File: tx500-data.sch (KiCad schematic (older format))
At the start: 62 parts, among them J1 USB_C_Receptacle, J2 FTDI, J3 AUDIO, SW1 VCCIO, U1 TUSB2036, U2 FT232RL, U3 HS-100B, U4 TPS76333, U5 SN75240, U6 TPS2041, Y1 AWSCR-6.00CPLA

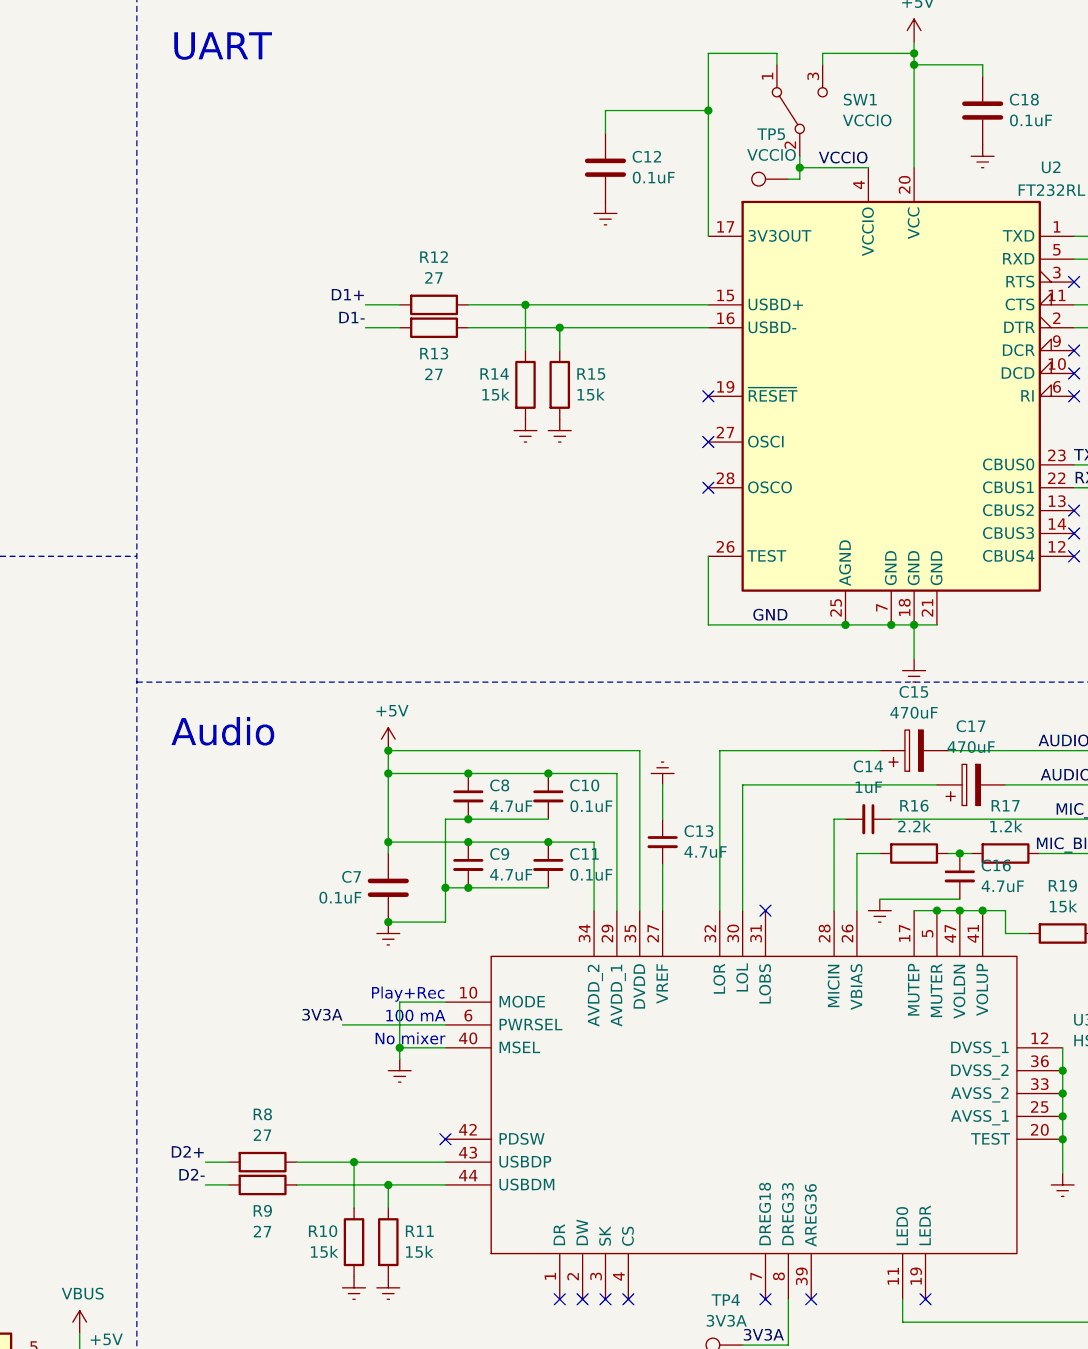
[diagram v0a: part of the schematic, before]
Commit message: Route most of the board
Still need to check design rules
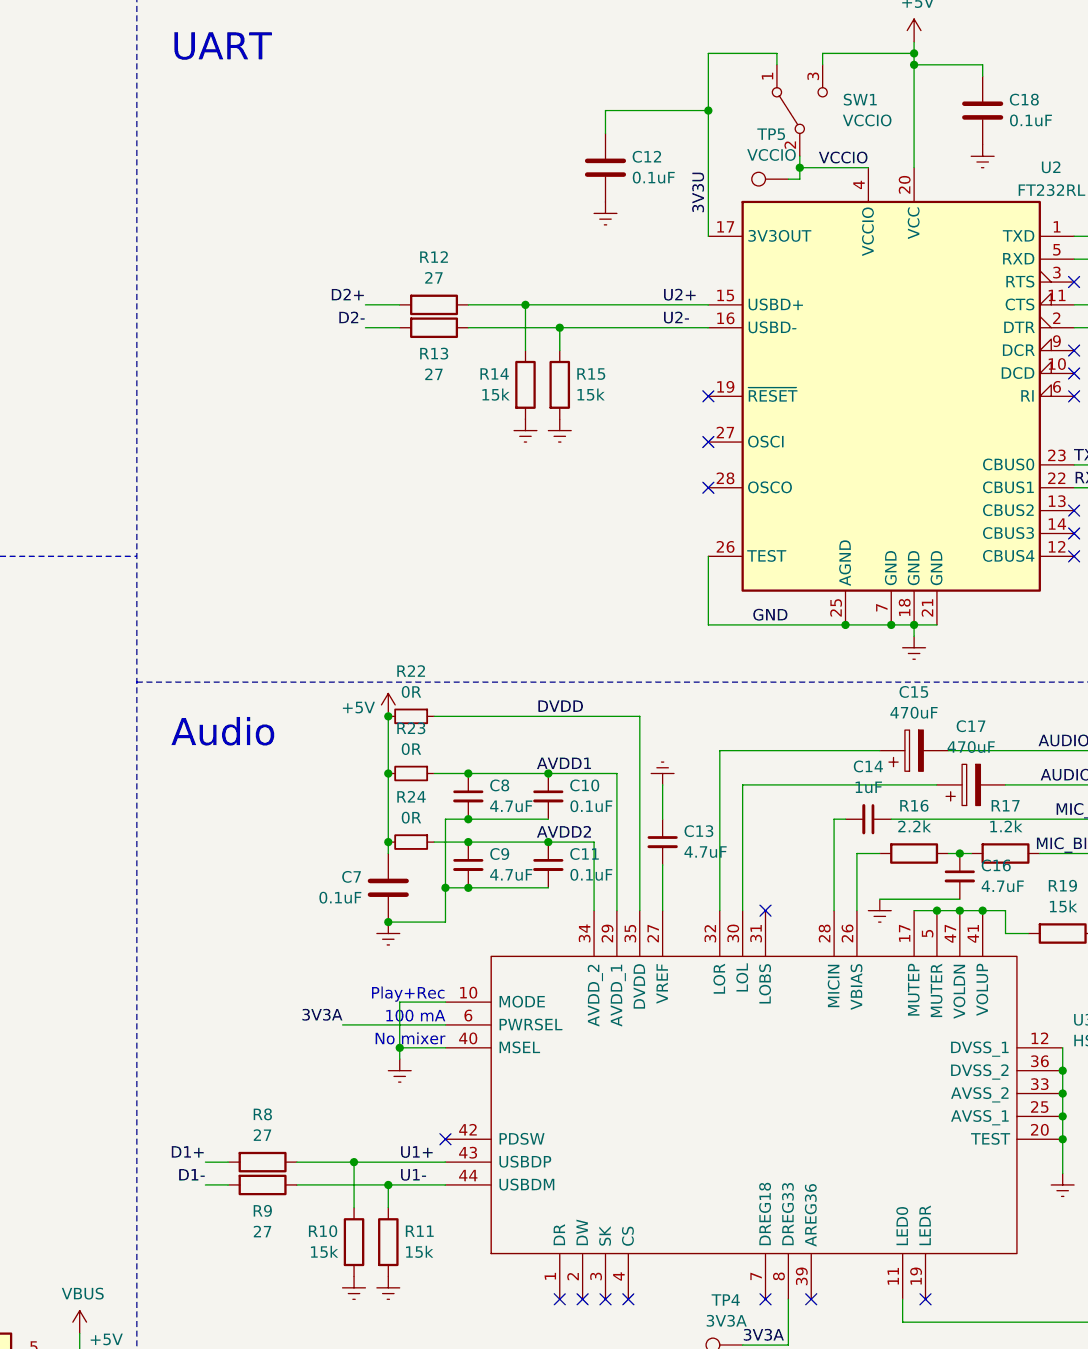
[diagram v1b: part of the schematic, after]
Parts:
- added R22, R23, R24: 0R, Resistor_SMD:R_0603_1608Metric, symbol Device:R_Small
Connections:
- net +5V: now also R22.2, R23.2, R24.2; no longer C10.1, C11.1, C8.1, C9.1, U3.29 (AVDD_1), U3.34 (AVDD_2), U3.35 (DVDD)
- net D1+: now also R8.2; no longer R12.2
- net D1-: now also R9.2; no longer R13.2
- net D2+: now also R12.2; no longer R8.2
- net D2-: now also R13.2; no longer R9.2
- net U2+: now reaches R12.1, R14.1, U2.15 (USBD+)
- net U2-: now reaches R13.1, R15.1, U2.16 (USBD-)
- net U1+: now reaches R10.1, R8.1, U3.43 (USBDP)
- net U1-: now reaches R11.1, R9.1, U3.44 (USBDM)
- net 3V3U: now reaches C12.1, SW1.1 (A), U2.17 (3V3OUT)
- new net AVDD1: C10.1, C8.1, R23.1, U3.29 (AVDD_1)
- new net AVDD2: C11.1, C9.1, R24.1, U3.34 (AVDD_2)
- new net DVDD: R22.1, U3.35 (DVDD)
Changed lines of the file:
@@
 L power:GNDREF #PWR?
 U 1 1 605FD4DB
-P 8950 3400
+P 8950 3300
 AR Path="/6059C0E9/605FD4DB" Ref="#PWR?"  Part="1"
 AR Path="/605FD4DB" Ref="#PWR033"  Part="1"
-F 0 "#PWR033" H 8950 3150 50  0001 C CNN
-F 1 "GNDREF" H 8955 3227 50  0001 C CNN
-F 2 "" H 8950 3400 50  0001 C CNN
-F 3 "" H 8950 3400 50  0001 C CNN
-	1    8950 3400
+F 0 "#PWR033" H 8950 3050 50  0001 C CNN
+F 1 "GNDREF" H 8955 3127 50  0001 C CNN
+F 2 "" H 8950 3300 50  0001 C CNN
+F 3 "" H 8950 3300 50  0001 C CNN
+	1    8950 3300
 	1    0    0    -1
 $EndComp
@@
 Text Label 10650 1550 2    50   ~ 0
 GND
-Text Label 6550 1950 2    50   ~ 0
+Text Label 5850 5700 2    50   ~ 0
 D1-
-Text Label 6550 1850 2    50   ~ 0
+Text Label 5850 5600 2    50   ~ 0
 D1+
 Text Label 4000 5600 0    50   ~ 0
@@
 Text Label 10550 4350 2    50   ~ 0
 MIC_IN
-Text Label 5850 5600 2    50   ~ 0
+Text Label 6550 1850 2    50   ~ 0
 D2+
-Text Label 5850 5700 2    50   ~ 0
+Text Label 6550 1950 2    50   ~ 0
 D2-
 Text Notes 5700 3800 0    118  ~ 0
@@
 	6250 5600 6500 5600
 Wire Wire Line
-	8950 3250 8950 3400
-Wire Wire Line
-	6650 3800 6650 3900
+	8950 3250 8950 3300
+Wire Wire Line
+	6650 3650 6650 3900
 Wire Wire Line
 	8400 6400 8200 6400
@@
 L power:+5V #PWR023
 U 1 1 609E6767
-P 6650 3800
-F 0 "#PWR023" H 6650 3650 50  0001 C CNN
-F 1 "+5V" H 6665 3973 50  0000 C CNN
-F 2 "" H 6650 3800 50  0001 C CNN
-F 3 "" H 6650 3800 50  0001 C CNN
-	1    6650 3800
+P 6650 3650
+F 0 "#PWR023" H 6650 3500 50  0001 C CNN
+F 1 "+5V" H 6592 3687 50  0000 R CNN
+F 2 "" H 6650 3650 50  0001 C CNN
+F 3 "" H 6650 3650 50  0001 C CNN
+	1    6650 3650
 	1    0    0    -1
 $EndComp
@@
 	9350 3950 9800 3950
 Wire Wire Line
-	6650 3800 7750 3800
-Wire Wire Line
-	7750 3800 7750 4500
-Connection ~ 6650 3800
+	7750 3650 7750 4500
+Connection ~ 6650 3650
 Text Label 9800 4100 2    50   ~ 0
 MIC_IN
@@
 	1    0    0    -1
 $EndComp
-Wire Wire Line
-	6650 3900 7000 3900
 Connection ~ 7000 3900
 Wire Wire Line
@@
 	1    0    0    -1
 $EndComp
-Wire Wire Line
-	6650 4200 7000 4200
 Wire Wire Line
 	7550 4200 7550 4500
@@
 $EndComp
 Connection ~ 5400 6650
+$Comp
+L Device:R_Small R22
+U 1 1 60953C75
+P 6750 3650
+F 0 "R22" V 6554 3650 50  0000 C CNN
+F 1 "0R" V 6645 3650 50  0000 C CNN
+F 2 "Resistor_SMD:R_0603_1608Metric" H 6750 3650 50  0001 C CNN
+F 3 "~" H 6750 3650 50  0001 C CNN
+	1    6750 3650
+	0    1    1    0
+$EndComp
+Wire Wire Line
+	6850 3650 7750 3650
+$Comp
+L Device:R_Small R23
+U 1 1 609546BE
+P 6750 3900
+F 0 "R23" V 6554 3900 50  0000 C CNN
+F 1 "0R" V 6645 3900 50  0000 C CNN
+F 2 "Resistor_SMD:R_0603_1608Metric" H 6750 3900 50  0001 C CNN
+F 3 "~" H 6750 3900 50  0001 C CNN
+	1    6750 3900
+	0    1    1    0
+$EndComp
+Wire Wire Line
+	6850 3900 7000 3900
+$Comp
+L Device:R_Small R24
+U 1 1 60954ABD
+P 6750 4200
+F 0 "R24" V 6554 4200 50  0000 C CNN
+F 1 "0R" V 6645 4200 50  0000 C CNN
+F 2 "Resistor_SMD:R_0603_1608Metric" H 6750 4200 50  0001 C CNN
+F 3 "~" H 6750 4200 50  0001 C CNN
+	1    6750 4200
+	0    1    1    0
+$EndComp
+Wire Wire Line
+	6850 4200 7000 4200
+Text Label 7300 3650 0    50   ~ 0
+DVDD
+Text Label 7300 3900 0    50   ~ 0
+AVDD1
+Text Label 7300 4200 0    50   ~ 0
+AVDD2
+Text Label 7850 1850 0    50   ~ 0
+U2+
+Text Label 7850 1950 0    50   ~ 0
+U2-
+Text Label 6700 5600 0    50   ~ 0
+U1+
+Text Label 6700 5700 0    50   ~ 0
+U1-
+Text Label 8050 1450 1    50   ~ 0
+3V3U
 $EndSCHEMATC

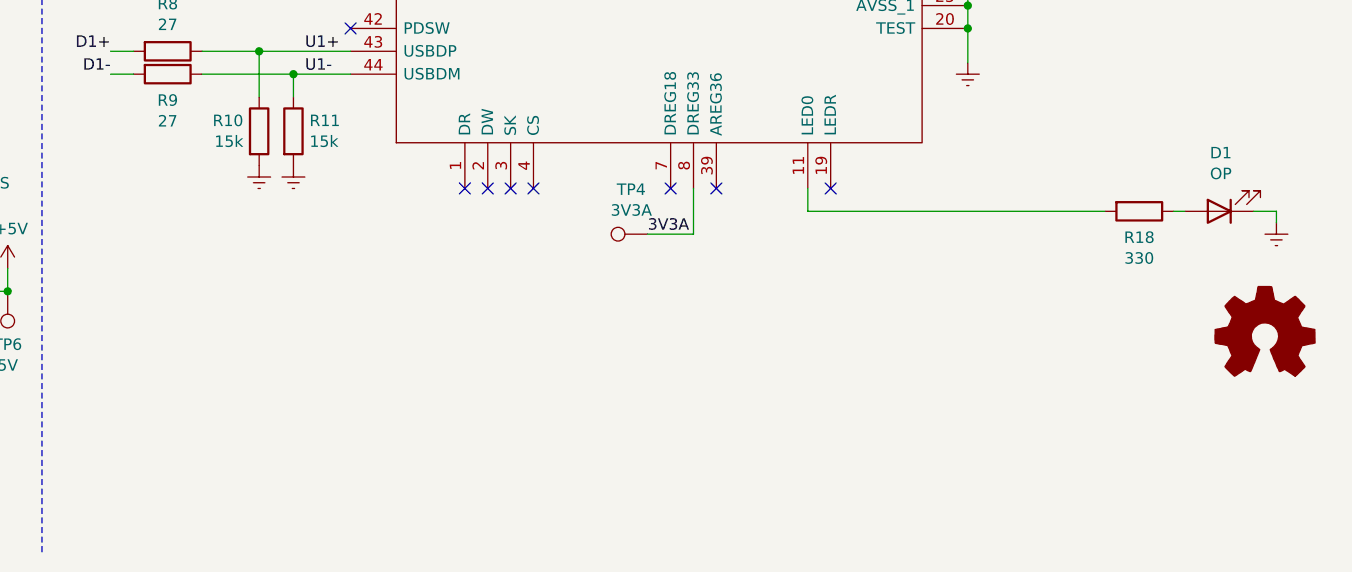
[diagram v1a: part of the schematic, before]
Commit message: Rotate UART and fix 3D images
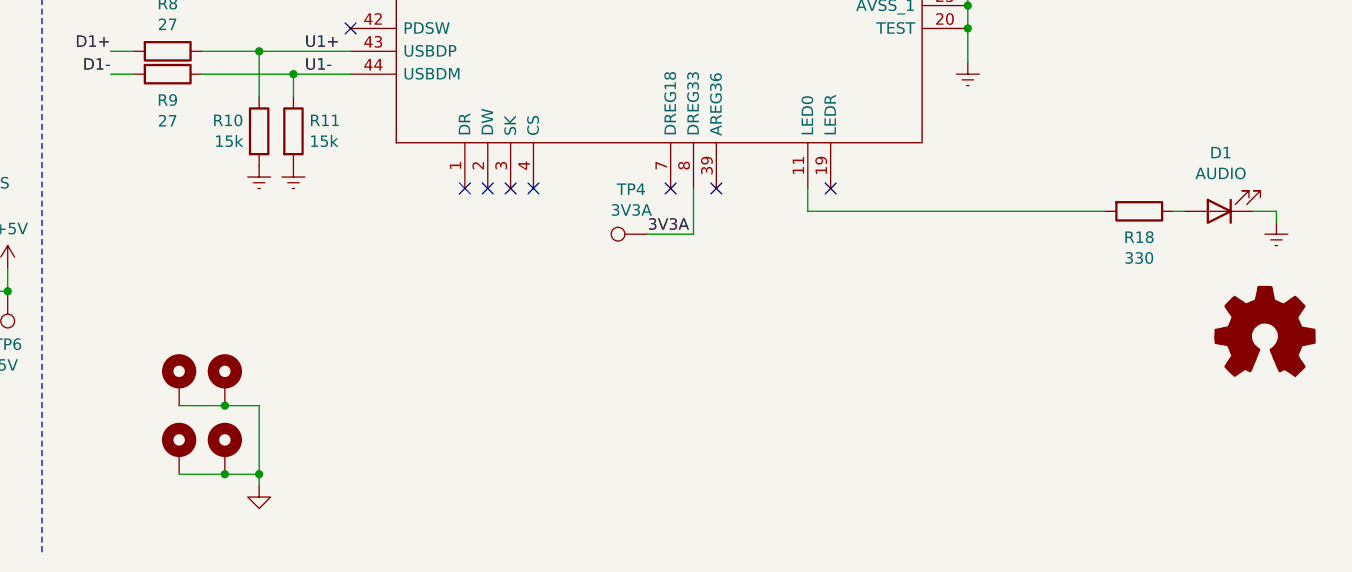
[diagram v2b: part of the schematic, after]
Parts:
- added H1, H2, H3, H4: MountingHole_Pad, MountingHole:MountingHole_2.2mm_M2_Pad, symbol Mechanical:MountingHole_Pad
- D1: value OP -> AUDIO
- J1: footprint CUI:UJ31-CH-G-SMT-TR-67 -> CUI:CUI_UJ31-CH-G-SMT-TR-67
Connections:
- net GND1: now also H1.1, H2.1, H3.1, H4.1
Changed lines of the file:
@@
 F 0 "J1" H 2307 2367 50  0000 C CNN
 F 1 "USB_C_Receptacle" H 2307 2276 50  0000 C CNN
-F 2 "CUI:UJ31-CH-G-SMT-TR-67" H 2350 1500 50  0001 C CNN
+F 2 "CUI:CUI_UJ31-CH-G-SMT-TR-67" H 2350 1500 50  0001 C CNN
 F 3 "https://www.mouser.com/datasheet/2/670/uj31_ch_g_smt_tr_67-2306975.pdf" H 2350 1500 50  0001 C CNN
 F 4 "CUI" H 2200 1500 50  0001 C CNN "Manufacturer"
@@
 P 10700 6300
 F 0 "D1" H 10693 6045 50  0000 C CNN
-F 1 "OP" H 10693 6136 50  0000 C CNN
+F 1 "AUDIO" H 10693 6136 50  0000 C CNN
 F 2 "LED_SMD:LED_0603_1608Metric" H 10700 6300 50  0001 C CNN
 F 3 "" H 10700 6300 50  0001 C CNN
@@
 Text Label 8050 1450 1    50   ~ 0
 3V3U
+$Comp
+L Mechanical:MountingHole_Pad H3
+U 1 1 6098967B
+P 6350 7050
+F 0 "H3" H 6350 7337 50  0001 C CNN
+F 1 "MountingHole_Pad" H 6350 7246 50  0001 C CNN
+F 2 "MountingHole:MountingHole_2.2mm_M2_Pad" H 6350 7050 50  0001 C CNN
+F 3 "~" H 6350 7050 50  0001 C CNN
+	1    6350 7050
+	1    0    0    -1
+$EndComp
+$Comp
+L Mechanical:MountingHole_Pad H1
+U 1 1 60989F62
+P 6150 7050
+F 0 "H1" H 6250 7099 50  0001 L CNN
+F 1 "MountingHole_Pad" H 6250 7008 50  0001 L CNN
+F 2 "MountingHole:MountingHole_2.2mm_M2_Pad" H 6150 7050 50  0001 C CNN
+F 3 "~" H 6150 7050 50  0001 C CNN
+	1    6150 7050
+	1    0    0    -1
+$EndComp
+$Comp
+L Mechanical:MountingHole_Pad H4
+U 1 1 6098A40D
+P 6350 7350
+F 0 "H4" H 6450 7399 50  0001 L CNN
+F 1 "MountingHole_Pad" H 6450 7308 50  0001 L CNN
+F 2 "MountingHole:MountingHole_2.2mm_M2_Pad" H 6350 7350 50  0001 C CNN
+F 3 "~" H 6350 7350 50  0001 C CNN
+	1    6350 7350
+	1    0    0    -1
+$EndComp
+$Comp
+L Mechanical:MountingHole_Pad H2
+U 1 1 6098A95D
+P 6150 7350
+F 0 "H2" H 6250 7399 50  0001 L CNN
+F 1 "MountingHole_Pad" H 6250 7308 50  0001 L CNN
+F 2 "MountingHole:MountingHole_2.2mm_M2_Pad" H 6150 7350 50  0001 C CNN
+F 3 "~" H 6150 7350 50  0001 C CNN
+	1    6150 7350
+	1    0    0    -1
+$EndComp
+$Comp
+L power:GND1 #PWR0101
+U 1 1 60990A0B
+P 6500 7500
+F 0 "#PWR0101" H 6500 7250 50  0001 C CNN
+F 1 "GND1" H 6505 7327 50  0001 C CNN
+F 2 "" H 6500 7500 50  0001 C CNN
+F 3 "" H 6500 7500 50  0001 C CNN
+	1    6500 7500
+	1    0    0    -1
+$EndComp
+Wire Wire Line
+	6150 7150 6350 7150
+Wire Wire Line
+	6500 7150 6500 7450
+Connection ~ 6350 7150
+Wire Wire Line
+	6350 7150 6500 7150
+Wire Wire Line
+	6150 7450 6350 7450
+Connection ~ 6500 7450
+Wire Wire Line
+	6500 7450 6500 7500
+Connection ~ 6350 7450
+Wire Wire Line
+	6350 7450 6500 7450
 $EndSCHEMATC

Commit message: Start prepping fabrication
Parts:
- C1, C12, C3: Description - -> (none); LCSC (none) -> C1588
- C10, C11, C18, C7: LCSC (none) -> C1588
- C13, C16, C8, C9: LCSC (none) -> C19666
- C14: LCSC (none) -> C15849
- C15, C17, H1, H2, H3, H4, J2, J3, LOGO1, SW1, TP1, TP2, TP3, TP4, TP5, TP6, U1, U4, U5: LCSC (none) -> -
- C2, C4: Description - -> (none); LCSC (none) -> C19666
- C5, C6: Description - -> (none); LCSC (none) -> C1653
- D1, D2, D3: LCSC (none) -> C2286
- J1: LCSC (none) -> -; Manufacturer CUI -> (none); Manufacturer_Name (none) -> CUI; Manufacturer_Part_Number (none) -> UJ31-CH-G-SMT-TR-67; Mfg Part # UJ31-CH-G-SMT-TR-67 -> (none)
- L1, L2: footprint Inductor_SMD:L_0603_1608Metric -> Inductor_SMD:L_0805_2012Metric; LCSC (none) -> C1017
- R1, R10, R11, R14, R15, R19: Description - -> (none); LCSC (none) -> C22809
- R12, R13, R6, R7, R8, R9: Description - -> (none); LCSC (none) -> C25190
- R16: Description - -> (none); LCSC (none) -> C4190
- R17: Description - -> (none); LCSC (none) -> C22765
- R18, R20, R21: LCSC (none) -> C23137
- R2, R3: Description - -> (none); LCSC (none) -> C22843
- R22, R23, R24: LCSC (none) -> C21189
- R4, R5: LCSC (none) -> C23186
- U2: LCSC (none) -> C8690
- U3: Height 1.6 -> (none); LCSC (none) -> -
- U6: Description (none) -> Overcurrent protection; LCSC (none) -> -
- Y1: Description Resonators 6.0 MHZ 30PF -> Resonator 6 MHz; Height 1.7 -> (none); LCSC (none) -> -; Mouser Part Number 815-CR-6.00CPLA-30-T -> (none); Mouser Price/Stock https://www.mouser.co.uk/ProductDetail/ABRACON/AWSCR-600CPL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 -> (none)

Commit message: Add more LCSC part numbers
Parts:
- C15, C17: LCSC - -> C232200
- J2, J3: LCSC - -> C471518
- SW1: LCSC - -> C221660
- U1: LCSC - -> C43665
- U3: LCSC - -> C371351
- U4: LCSC - -> C7100
- U5: LCSC - -> C7067
- U6: LCSC - -> C206041
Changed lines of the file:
@@
 F 9 "" H 3000 7781 50  0001 C CNN "Vendor"
 F 10 "" H 3550 7600 50  0001 C CNN "quantity"
-F 11 "-" H 3000 5900 50  0001 C CNN "LCSC"
+F 11 "C43665" H 3000 5900 50  0001 C CNN "LCSC"
 	1    3000 5900
 	1    0    0    -1
@@
 F 9 "" H 3350 4142 50  0001 C CNN "Vendor"
 F 10 "" H 3350 4142 50  0001 C CNN "quantity"
-F 11 "-" H 3350 3700 50  0001 C CNN "LCSC"
+F 11 "C7100" H 3350 3700 50  0001 C CNN "LCSC"
 	1    3350 3700
 	1    0    0    -1
@@
 F 10 "" H 7500 6750 50  0001 C CNN "Vendor"
 F 11 "" H 8921 4356 50  0001 C CNN "quantity"
-F 12 "-" H 7700 6200 50  0001 C CNN "LCSC"
+F 12 "C371351" H 7700 6200 50  0001 C CNN "LCSC"
 	1    7700 6200
 	0    -1   -1   0
@@
 F 9 "" H 3700 2725 50  0001 C CNN "Vendor"
 F 10 "" H 3700 2725 50  0001 C CNN "quantity"
-F 11 "-" H 3700 2400 50  0001 C CNN "LCSC"
+F 11 "C7067" H 3700 2400 50  0001 C CNN "LCSC"
 	1    3700 2400
 	1    0    0    -1
@@
 F 5 "TPS2041CDBV" H 4700 6650 50  0001 C CNN "Manufacturer_Part_Number"
 F 6 "Overcurrent protection" H 4700 6650 50  0001 C CNN "Description"
-F 7 "-" H 4700 6650 50  0001 C CNN "LCSC"
+F 7 "C206041" H 4700 6650 50  0001 C CNN "LCSC"
 	1    4700 6650
 	1    0    0    -1
@@
 F 2 "Connector_JST:JST_PH_B6B-PH-SM4-TB_1x06-1MP_P2.00mm_Vertical" H 10850 1750 50  0001 C CNN
 F 3 "" H 10850 1750 50  0001 C CNN
-F 4 "-" H 10850 1750 50  0001 C CNN "LCSC"
+F 4 "C471518" H 10850 1750 50  0001 C CNN "LCSC"
 	1    10850 1750
 	1    0    0    -1
@@
 F 2 "Connector_JST:JST_PH_B6B-PH-SM4-TB_1x06-1MP_P2.00mm_Vertical" H 10750 4050 50  0001 C CNN
 F 3 "" H 10750 4050 50  0001 C CNN
-F 4 "-" H 10750 4050 50  0001 C CNN "LCSC"
+F 4 "C471518" H 10750 4050 50  0001 C CNN "LCSC"
 	1    10750 4050
 	1    0    0    -1
@@
 F 2 "Button_Switch_SMD:SW_SPDT_CK-JS102011SAQN" H 8450 1000 50  0001 C CNN
 F 3 "" H 8450 1000 50  0001 C CNN
-F 4 "-" H 8450 1000 50  0001 C CNN "LCSC"
+F 4 "C221660" H 8450 1000 50  0001 C CNN "LCSC"
 	1    8450 1000
 	0    -1   -1   0
@@
 F 2 "Vishay:CAPPM7343X430N" H 8988 3650 50  0001 C CNN
 F 3 "" H 8950 3800 50  0001 C CNN
-F 4 "-" H 8950 3800 50  0001 C CNN "LCSC"
+F 4 "C232200" H 8950 3800 50  0001 C CNN "LCSC"
 	1    8950 3800
 	0    -1   -1   0
@@
 F 2 "Vishay:CAPPM7343X430N" H 9238 3800 50  0001 C CNN
 F 3 "" H 9200 3950 50  0001 C CNN
-F 4 "-" H 9200 3950 50  0001 C CNN "LCSC"
+F 4 "C232200" H 9200 3950 50  0001 C CNN "LCSC"
 	1    9200 3950
 	0    -1   -1   0

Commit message: Add BOM
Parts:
- C1, C10, C11, C12, C18, C3, C7: Vendor (none) -> LCSC; Vendor Part Number (none) -> C1588
- C13, C16, C2, C4, C8, C9: Vendor (none) -> LCSC; Vendor Part Number (none) -> C19666
- C14: Vendor (none) -> LCSC; Vendor Part Number (none) -> C15849
- C15, C17: Manufacturer_Name (none) -> Vishay; Manufacturer_Part_Number (none) -> 293D477X9010E2TE3; Vendor (none) -> Mouser; Vendor Part Number (none) -> 74-293D477X9010E2TE3
- C5, C6: Vendor (none) -> LCSC; Vendor Part Number (none) -> C1653
- D1, D2, D3: Vendor (none) -> LCSC; Vendor Part Number (none) -> C2286
- H1, H2, H3, H4, LOGO1, TP1, TP2, TP3, TP4, TP5, TP6: Manufacturer_Name (none) -> -; Manufacturer_Part_Number (none) -> -; Vendor (none) -> -; Vendor Part Number (none) -> -
- J1: Vendor (none) -> Mouser; Vendor Part Number (none) -> 490-UJ31-CH-GSMTTR67
- J2, J3: Manufacturer_Name (none) -> JST; Manufacturer_Part_Number (none) -> B6B-PH-SM4-TB; Vendor (none) -> Newark; Vendor Part Number (none) -> 37K9975
- L1, L2: Vendor (none) -> LCSC; Vendor Part Number (none) -> C1017
- R1, R10, R11, R14, R15, R19: Vendor (none) -> LCSC; Vendor Part Number (none) -> C22809
- R12, R13, R6, R7, R8, R9: value 27 -> 27R; Vendor (none) -> LCSC; Vendor Part Number (none) -> C25190
- R16: Vendor (none) -> LCSC; Vendor Part Number (none) -> C4190
- R17: Vendor (none) -> LCSC; Vendor Part Number (none) -> C22765
- R18, R20, R21: value 330 -> 330R; Vendor (none) -> LCSC; Vendor Part Number (none) -> C23137
- R2, R3: Vendor (none) -> LCSC; Vendor Part Number (none) -> C22843
- R22, R23, R24: Vendor (none) -> LCSC; Vendor Part Number (none) -> C21189
- R4, R5: Vendor (none) -> LCSC; Vendor Part Number (none) -> C23186
- SW1: Manufacturer_Name (none) -> C&K; Manufacturer_Part_Number (none) -> JS102011SAQN; Vendor (none) -> Mouser; Vendor Part Number (none) -> 611-JS102011SAQN
- U1: Vendor (none) -> Mouser; Vendor Part Number (none) -> 595-TUSB2036VFRG4
- U2: Vendor (none) -> LCSC; Vendor Part Number (none) -> C8690
- U3: Vendor (none) -> Symmetry; Vendor Part Number (none) -> HS-100B
- U4: Vendor (none) -> LCSC; Vendor Part Number (none) -> C7100
- U5: Vendor (none) -> LCSC; Vendor Part Number (none) -> C7067
- U6: Vendor (none) -> LCSC; Vendor Part Number (none) -> C206041
- Y1: Vendor (none) -> Mouser; Vendor Part Number (none) -> 815-CR-6.00CPLA-30-T
